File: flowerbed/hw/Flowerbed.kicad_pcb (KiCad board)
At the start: 2 copper layers, 18.5 x 19.7 mm, 24 parts, among them J1 Conn_01x04, J2 Conn_01x04, U1 STM32G030F6Px, U2 VL53L0X, U3 W25Q16JVSS, U4 MAX98357AETE+, X1 12.288MHz

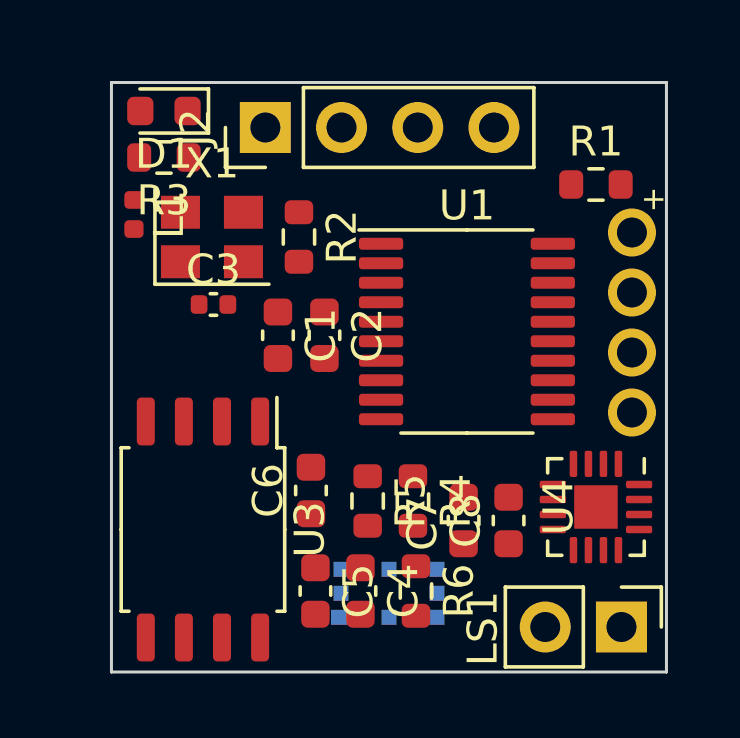
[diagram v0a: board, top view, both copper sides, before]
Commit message: Revise flowerbed unit layout
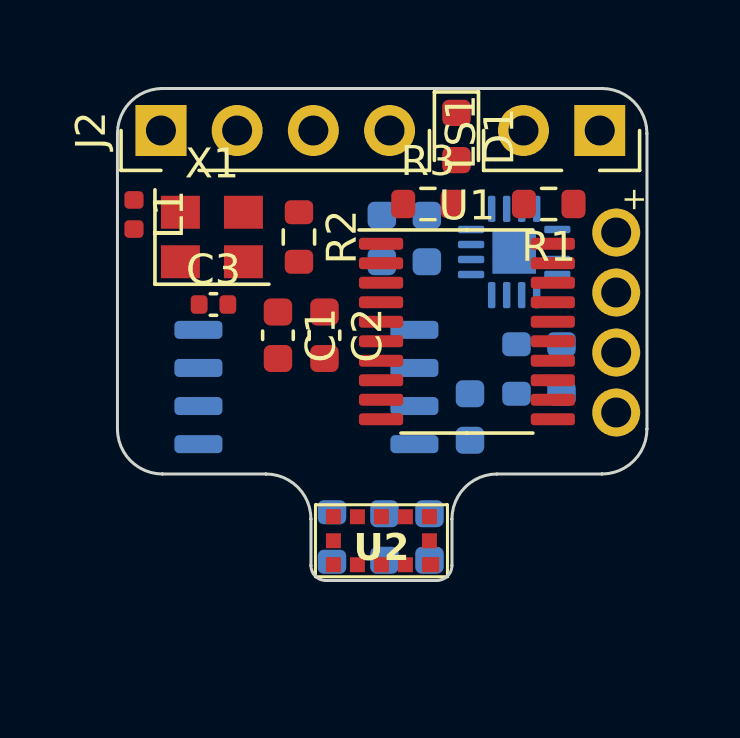
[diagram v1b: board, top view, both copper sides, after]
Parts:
- C4, C5, C6, C7, C8, R4, R5, R6, U3, U4: moved to B.Cu
- U2: moved to F.Cu
- moved LS1 16.6 mm to (60.9, 28.3)
- moved C7 9.79 mm to (53.6, 31.9), turned to -90 degrees
- moved C8 9.79 mm to (55.1, 31.9), turned to -90 degrees
- moved D1 9.79 mm to (56.1, 28.5), turned to -90 degrees
- moved R3 8.94 mm to (55.1, 30.8), turned to 0 degrees
- moved U4 8.93 mm to (58.0, 32.4), turned to 90 degrees
- moved R5 7.82 mm to (59.6, 36.2)
- moved U3 5.87 mm to (51.1, 36.9), turned to 0 degrees
- moved C6 5.84 mm to (56.5, 37.9)
- moved R4 5.59 mm to (58.1, 36.2)
- moved C5 4.20 mm to (55.2, 41.9)
- moved J2 3.48 mm to (46.2, 28.3)
- moved R6 3.33 mm to (52.0, 41.9)
- moved C4 1.97 mm to (53.7, 41.9)
- moved U2 1.77 mm to (53.6, 42.2), turned to 0 degrees
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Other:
- board size 18.5 x 19.7 mm -> 17.7 x 16.4 mm

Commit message: (WIP) Add flowerbed central schematic
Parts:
- renumbered J2 to J1, J1 to J2
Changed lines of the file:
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@@
     (property "ki_keywords" "connector")
     (attr through_hole)
-    (fp_text reference "J2" (at 0 -2.33 90) (layer "F.SilkS")
+    (fp_text reference "J1" (at 0 -2.33 90) (layer "F.SilkS")
         (effects (font (size 1 1) (thickness 0.15)))
     )
@@
     (property "ki_keywords" "connector")
     (attr smd)
-    (fp_text reference "J1" (at 0 -0.5 -90 unlocked) (layer "F.SilkS") hide
+    (fp_text reference "J2" (at 0 -0.5 -90 unlocked) (layer "F.SilkS") hide
         (effects (font (size 1 1) (thickness 0.1)))
     )

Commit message: Route flowerbed unit (!)
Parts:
- C4, C5: footprint Capacitor_SMD:C_0603_1608Metric -> Capacitor_SMD:C_0402_1005Metric
- U4: footprint Package_DFN_QFN:QFN-16-1EP_3x3mm_P0.5mm_EP1.45x1.45mm -> Flowerbed_footprints:QFN-16_3x3mm_P0.5mm
- moved R5 2.19 mm to (58.0, 37.8), turned to 90 degrees
- moved R4 2.12 mm to (59.5, 37.8), turned to 90 degrees
- moved C4 0.63 mm to (54.2, 41.5)
- moved C5 0.30 mm to (55.2, 41.5)
- moved R6 0.25 mm to (52.2, 41.9)
- moved J2 0.18 mm to (61.6, 34.7)
- moved C6 0.05 mm to (56.5, 37.8)
- moved U1 0.05 mm to (56.4, 35.0)
- moved U3 0.05 mm to (51.1, 36.8)
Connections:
- U1 pad 8: SPI2_CSx -> unconnected-(U1-PA1-Pad8)
- U1 pad 9: unconnected-(U1-PA2-Pad9) -> SPI2_CSx
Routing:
- net VDD: track 0.00 -> 72.0 mm, vias 0 -> 4
- net I2C2_SDA: track 0.00 -> 19.3 mm, vias 0 -> 1
- net I2C2_SCL: track 0.00 -> 18.5 mm, vias 0 -> 1
- net I2C1_SCL: track 0.00 -> 12.4 mm
- net SWCLK: track 0.00 -> 7.20 mm
- net SPI2_CSx: track 0.00 -> 6.66 mm, vias 0 -> 1
- net SPI2_MISO: track 0.00 -> 6.24 mm, vias 0 -> 1
- net Net-(U2-XSHUT): track 0.00 -> 6.23 mm, vias 0 -> 1
- net SPI2_MOSI: track 0.00 -> 6.02 mm, vias 0 -> 1
- net SWDIO: track 0.00 -> 5.65 mm
- net I2S1_CK: track 0.00 -> 5.42 mm, vias 0 -> 1
- net I2S1_WS: track 0.00 -> 4.69 mm, vias 0 -> 1
- net Net-(U4-OUTN): track 0.00 -> 4.64 mm
- net I2C1_SDA: track 0.00 -> 3.91 mm
- net ACT_LED: track 0.00 -> 3.61 mm
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- added copper zone on B.Cu, net GND
- added copper zone on F.Cu, net GND
- added copper zone on F.Cu, net Net-(X1-EN)
- added copper zone on B.Cu, net VDD

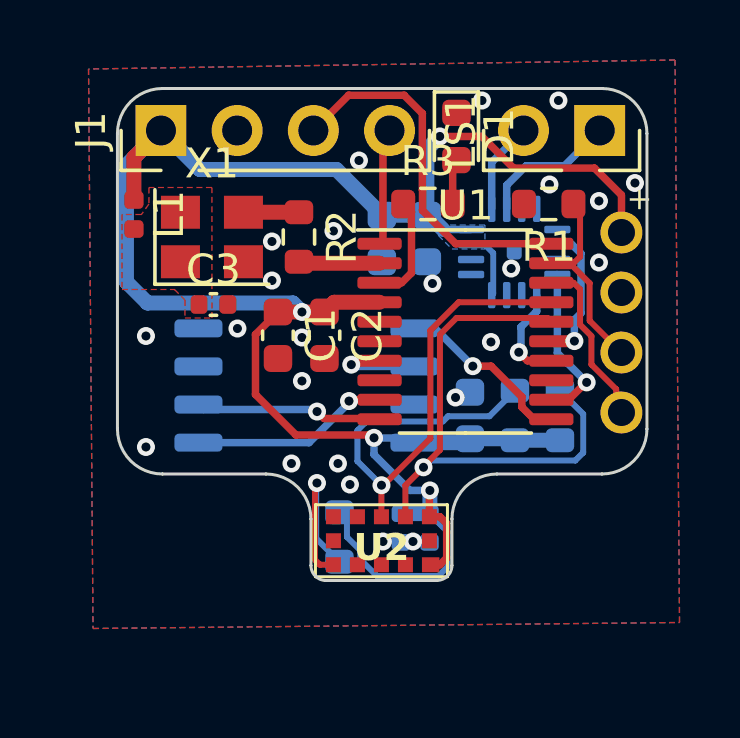
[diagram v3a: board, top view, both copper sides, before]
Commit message: Finalize flowerbed unit PCB design
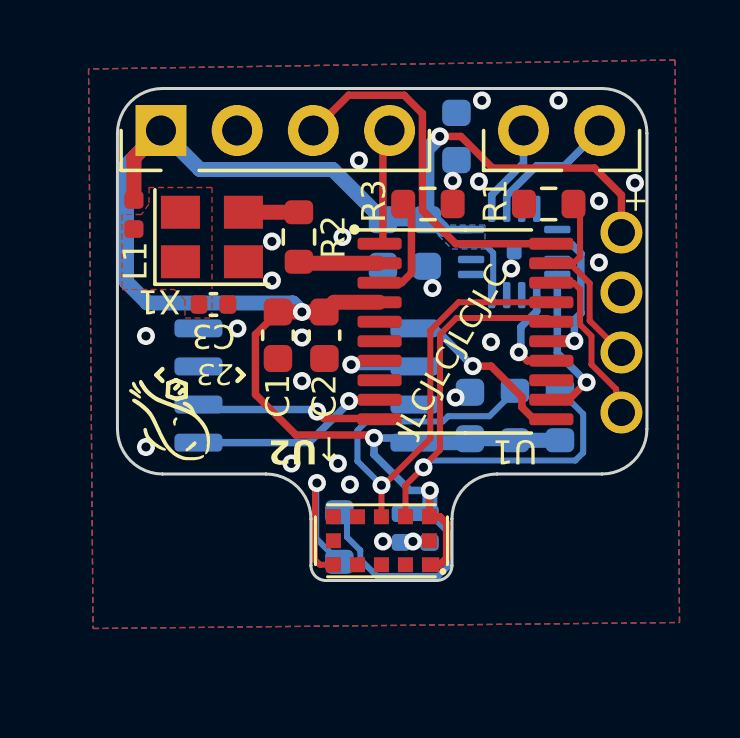
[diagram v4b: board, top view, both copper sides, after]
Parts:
- added G***: LOGO, LOGO, F.Cu at (46.5, 37.9)
- added G***: LOGO, LOGO, B.Cu at (46.5, 32.2)
- D1: moved to B.Cu
- moved C7 0.15 mm to (53.6, 32.0)
- moved C8 0.15 mm to (55.1, 32.0)
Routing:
- net Net-(D1-A): vias 0 -> 1
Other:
- board text added: "23"
- board text added: "BEEPBUG Rev. U1"
- board text added: "GND"
- board text added: "JLCJLCJLCJLC"
- board text added: "SCL"
- board text added: "SDA"
- board text added: "VCC"
- board text added: "↓"
